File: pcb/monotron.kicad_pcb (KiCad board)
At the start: 2 copper layers, 38 parts, among them J1 Mono / Stereo, J10 DB25_Female, J11 Mini-DIN-6, J12 Mini-DIN-6, J2 AudioJack3, J3 Jack-DC, J4 DB9_Male, J5 01x07 SD Interface, J6 DB15_Female_HighDensity_Mount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, J7 2x6 UART Bridge, J8 1x4 I2C Expansion Connector, J9 DB9_Male, U1 TM4C123G_Launchpad, U2 MAX3232, U3 ATmega48A-PU

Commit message: Updated footprints.
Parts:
- added C15: 100n, Capacitor_THT:C_Disc_D5.0mm_W2.5mm_P2.50mm, F.Cu at (329.6, 106.9)
- added D1: 1N4148, Diode_THT:D_A-405_P12.70mm_Horizontal, F.Cu at (302.6, 135.2)
- added J13: DB25_Female, Connector_Dsub:DSUB-25_Male_Horizontal_P2.77x2.84mm_EdgePinOffset7.70mm_Housed_MountingHolesOffset9.12mm, F.Cu at (94.1, 144.5)
- added J14: Mini-DIN-6, Launchpad:mini-DIN 6, F.Cu at (52.7, 22.6)
- added J15: Mini-DIN-6, Launchpad:mini-DIN 6, F.Cu at (76.3, 22.7)
- added R10: 220, Resistor_THT:R_Axial_DIN0411_L9.9mm_D3.6mm_P12.70mm_Horizontal, F.Cu at (287.2, 139.8)
- added R11: 220, Resistor_THT:R_Axial_DIN0411_L9.9mm_D3.6mm_P12.70mm_Horizontal, F.Cu at (302.9, 131.5)
- added R12: 220, Resistor_THT:R_Axial_DIN0411_L9.9mm_D3.6mm_P12.70mm_Horizontal, F.Cu at (287.2, 144.0)
- added R13: 220, Resistor_THT:R_Axial_DIN0411_L9.9mm_D3.6mm_P12.70mm_Horizontal, F.Cu at (287.2, 127.4)
- added R14: 220, Resistor_THT:R_Axial_DIN0411_L9.9mm_D3.6mm_P12.70mm_Horizontal, F.Cu at (287.2, 135.7)
- added R15: 10K, Resistor_THT:R_Axial_DIN0411_L9.9mm_D3.6mm_P12.70mm_Horizontal, F.Cu at (302.9, 127.4)
- added R16: 470, Resistor_THT:R_Axial_DIN0411_L9.9mm_D3.6mm_P12.70mm_Horizontal, F.Cu at (287.2, 131.5)
- added U4: 6N138, Package_DIP:DIP-8_W7.62mm, F.Cu at (302.5, 138.4)
- added U5: ATmega48A-PU, Package_DIP:DIP-28_W7.62mm, F.Cu at (341.1, 86.7)
- C10: value 100n -> 470n
- C7: value 470n -> 100n
- J10: value DB25_Female -> DIN-5_180degree; footprint Connector_Dsub:DSUB-25_Male_Horizontal_P2.77x2.84mm_EdgePinOffset7.70mm_Housed_MountingHolesOffset9.12mm -> Launchpad:5P180 DIN Socket
- J11: value Mini-DIN-6 -> DIN-5_180degree; footprint Connector_PinHeader_2.54mm:PinHeader_1x04_P2.54mm_Horizontal -> Launchpad:5P180 DIN Socket
- J12: value Mini-DIN-6 -> DB9_Male; footprint Connector_PinHeader_2.54mm:PinHeader_1x04_P2.54mm_Horizontal -> Connector_Dsub:DSUB-9_Male_Horizontal_P2.77x2.84mm_EdgePinOffset7.70mm_Housed_MountingHolesOffset9.12mm
- J2: value AudioJack3 -> Jack-DC; footprint Connector_Audio:Jack_3.5mm_CUI_SJ1-3533NG_Horizontal -> Connector_BarrelJack:BarrelJack_CUI_PJ-102AH_Horizontal
- J3: value Jack-DC -> 01x07 SD Interface; footprint Connector_BarrelJack:BarrelJack_CUI_PJ-102AH_Horizontal -> Connector_PinHeader_2.54mm:PinHeader_1x07_P2.54mm_Vertical
- J4: value DB9_Male -> AudioJack3; footprint Connector_Dsub:DSUB-9_Male_Horizontal_P2.77x2.84mm_EdgePinOffset7.70mm_Housed_MountingHolesOffset9.12mm -> Connector_Audio:Jack_3.5mm_CUI_SJ1-3533NG_Horizontal
- J5: value 01x07 SD Interface -> DB9_Male; footprint Connector_PinHeader_2.54mm:PinHeader_1x07_P2.54mm_Vertical -> Connector_Dsub:DSUB-9_Male_Horizontal_P2.77x2.84mm_EdgePinOffset7.70mm_Housed_MountingHolesOffset9.12mm
- J6: value DB15_Female_HighDensity_MountingHoles -> 1x4 I2C Expansion Connector; footprint Connector_Dsub:DSUB-15-HD_Female_Horizontal_P2.29x1.98mm_EdgePinOffset8.35mm_Housed_MountingHolesOffset10.89mm -> Connector_PinHeader_2.54mm:PinHeader_1x04_P2.54mm_Vertical
- J7: value 2x6 UART Bridge -> DB15_Female_HighDensity_MountingHoles; footprint Connector_PinHeader_2.54mm:PinHeader_2x06_P2.54mm_Vertical -> Connector_Dsub:DSUB-15-HD_Female_Horizontal_P2.29x1.98mm_EdgePinOffset8.35mm_Housed_MountingHolesOffset10.89mm
- J8: value 1x4 I2C Expansion Connector -> 2x6 UART Bridge; footprint Connector_PinHeader_2.54mm:PinHeader_1x04_P2.54mm_Vertical -> Connector_PinHeader_2.54mm:PinHeader_2x06_P2.54mm_Vertical
- J9: value DB9_Male -> DIN-5_180degree; footprint Connector_Dsub:DSUB-9_Male_Horizontal_P2.77x2.84mm_EdgePinOffset7.70mm_Housed_MountingHolesOffset9.12mm -> Launchpad:5P180 DIN Socket
- U3: value ATmega48A-PU -> 74LS14; footprint Package_DIP:DIP-28_W7.62mm -> Package_DIP:DIP-14_W7.62mm
- moved J10 242.3 mm to (18.2, 150.1)
- moved J3 219.3 mm to (-34.4, 86.4)
- moved J11 175.0 mm to (40.0, 149.5)
- moved J4 140.7 mm to (105.4, 94.7), turned to 270 degrees
- moved J7 140.3 mm to (92.1, 68.7), turned to 90 degrees
- moved J12 104.3 mm to (94.1, 179.2)
- moved J5 64.1 mm to (93.9, 45.3), turned to 90 degrees
- moved C10 59.1 mm to (185.1, 111.1)
- moved C1 59.1 mm to (202.0, 108.2)
- moved C2 59.1 mm to (207.5, 108.2)
- moved C8 59.1 mm to (196.2, 111.1)
- moved C9 59.1 mm to (190.6, 111.1)
- moved U1 51.1 mm to (57.5, 99.3)
- moved C12 46.0 mm to (143.4, 148.3)
- moved C14 35.9 mm to (122.8, 164.6)
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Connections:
- net Net-(R3-Pad1) renamed /PE4_AUDIO_L
- net Net-(R4-Pad1) renamed /PE5_AUDIO_R
- net Net-(U1-Pad2.2) renamed /PB2_SPARE
- net Net-(U1-Pad2.4) renamed /BUTTON_1
- net Net-(U1-Pad2.7) renamed /PB6_SPARE
- net Net-(U1-Pad3.5) renamed /PD2_SPARE
- net Net-(U1-Pad4.1) renamed /BLUE_LED
- net Net-(U1-Pad4.2) renamed /GREEN_LED
- net Net-(U1-Pad4.3) renamed /PB3_SPARE
- C10 pad 1: Net-(C10-Pad1) -> GND
- C10 pad 2: GND -> Net-(C10-Pad2)
- C7 pad 2: Net-(C7-Pad2) -> GND
- C8 pad 1: Net-(C10-Pad1) -> Net-(C8-Pad1)
- C9 pad 1: GND -> Net-(C7-Pad1)
- J10 pad 1: /Monotron I/O Expansion/STROBE -> Net-(J10-Pad1)
- J10 pad 2: /Monotron I/O Expansion/D0 -> GND
- J10 pad 3: /Monotron I/O Expansion/D1 -> Net-(J10-Pad3)
- J10 pad 4: /Monotron I/O Expansion/D2 -> Net-(J10-Pad4)
- J10 pad 5: /Monotron I/O Expansion/D3 -> Net-(J10-Pad5)
- J10 pad 6: /Monotron I/O Expansion/D4 -> (no net)
- J10 pad 7: /Monotron I/O Expansion/D5 -> (no net)
- J11 pad 1: /Monotron I/O Expansion/KB_DATA -> Net-(J11-Pad1)
- J11 pad 3: GND -> Net-(J11-Pad3)
- J11 pad 4: +5V -> Net-(J11-Pad4)
- J12 pad 1: /Monotron I/O Expansion/MS_DATA -> /DCD
- J12 pad 2: Net-(J12-Pad2) -> /RS232_RX
- J12 pad 3: GND -> /RS232_TX
- J12 pad 4: +5V -> /DTR
- J3 pad 1: +5V -> Net-(J3-Pad1)
- J3 pad 2: GND -> /PA4_SD_MISO
- J3 pad 3: (no net) -> GND
- J5 pad 1: Net-(J5-Pad1) -> /PE2_JS_UP
- J5 pad 2: /PA4_SD_MISO -> /PE3_JS_DOWN
- J5 pad 3: GND -> /PD6_JS_LEFT
- J5 pad 4: /PA2_SD_CLK -> /PD7_JS_RIGHT
- J5 pad 5: +3V3 -> Net-(J5-Pad5)
- J5 pad 6: /PA5_SD_MOSI -> /PF4_JS_FIRE
- J5 pad 7: /PA3_SD_CS -> Net-(J5-Pad7)
- J6 pad 1: Net-(J6-Pad1) -> GND
- J6 pad 2: Net-(J6-Pad2) -> +5V
- J6 pad 3: Net-(J6-Pad3) -> /PA7_I2C_SDA
- J6 pad 4: Net-(J6-Pad4) -> /PA6_I2C_SCL
- J7 pad 1: +3V3 -> Net-(J7-Pad1)
- J7 pad 10: /DTE_CTS -> Net-(J7-Pad10)
- J7 pad 11: GND -> Net-(J7-Pad11)
- J7 pad 12: GND -> Net-(J7-Pad12)
- J7 pad 2: Net-(C10-Pad1) -> Net-(J7-Pad2)
- J7 pad 3: /PB0_U1RX -> Net-(J7-Pad3)
- J7 pad 4: /DTE_RX -> Net-(J7-Pad4)
- J7 pad 5: /PB1_U1TX -> GND
- J7 pad 6: /DTE_TX -> GND
- J7 pad 7: /PC4_U1RTS -> GND
- J7 pad 8: /DTE_RTS -> GND
- J7 pad 9: /PC5_U1CTS -> Net-(J7-Pad9)
- J8 pad 1: GND -> +3V3
- J8 pad 2: +5V -> Net-(C7-Pad1)
- J8 pad 3: /PA7_I2C_SDA -> /PB0_U1RX
- J8 pad 4: /PA6_I2C_SCL -> /DTE_RX
- J9 pad 1: /DCD -> Net-(J9-Pad1)
- J9 pad 2: /RS232_RX -> GND
- J9 pad 3: /RS232_TX -> Net-(J9-Pad3)
- J9 pad 4: /DTR -> Net-(J9-Pad4)
- J9 pad 5: GND -> Net-(J9-Pad5)
- J9 pad 6: /DSR -> (no net)
- J9 pad 7: /RS232_RTS -> (no net)
- R7 pad 1: Net-(J6-Pad1) -> Net-(J7-Pad1)
- R8 pad 1: Net-(J6-Pad2) -> Net-(J7-Pad2)
- R9 pad 1: Net-(J6-Pad3) -> Net-(J7-Pad3)
- U1 pad 3.8: Net-(U1-Pad3.8) -> /PE2_JS_UP
- U1 pad 3.9: Net-(U1-Pad3.9) -> /PE3_JS_DOWN
- U1 pad 4.10: /PF4_FIRE -> /PF4_JS_FIRE
- U1 pad 4.6: /PC6_UP -> /PC6_MIDI_IN
- U1 pad 4.7: /PC7_DOWN -> /PC7_MIDI_OUT
- U1 pad 4.8: /PD6_LEFT -> /PD6_JS_LEFT
- U1 pad 4.9: /PD7_RIGHT -> /PD7_JS_RIGHT
- U2 pad 16: Net-(C10-Pad1) -> Net-(C7-Pad1)
- U2 pad 2: Net-(C8-Pad2) -> Net-(C9-Pad2)
- U2 pad 4: Net-(C7-Pad1) -> Net-(C8-Pad1)
- U2 pad 5: Net-(C7-Pad2) -> Net-(C8-Pad2)
- U2 pad 6: Net-(C9-Pad2) -> Net-(C10-Pad2)
- U3 pad 1: /Monotron I/O Expansion/SELPRIN -> /PC6_MIDI_IN
- U3 pad 10: /Monotron I/O Expansion/D7 -> (no net)
- U3 pad 11: /Monotron I/O Expansion/SEL -> (no net)
- U3 pad 12: /Monotron I/O Expansion/STROBE -> (no net)
- U3 pad 13: /Monotron I/O Expansion/AUTOF -> (no net)
- U3 pad 14: /Monotron I/O Expansion/D0 -> +5V
- U3 pad 2: /PE1_U7TX -> Net-(U3-Pad2)
- U3 pad 3: /PE0_U7RX -> Net-(U3-Pad2)
- U3 pad 4: /Monotron I/O Expansion/ACK -> Net-(R12-Pad1)
- U3 pad 5: /Monotron I/O Expansion/BUSY -> Net-(U3-Pad5)
- U3 pad 6: /Monotron I/O Expansion/PE -> Net-(R13-Pad2)
- U3 pad 7: +5V -> GND
- U3 pad 8: GND -> Net-(U3-Pad5)
- U3 pad 9: /Monotron I/O Expansion/D6 -> /PC7_MIDI_OUT

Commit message: Primary component layout complete.
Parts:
- removed C15: 100n, Capacitor_THT:C_Disc_D5.0mm_W2.5mm_P2.50mm
- J10: value DIN-5_180degree -> DIN5 MIDI Thru
- J11: value DIN-5_180degree -> DIN5 MIDI In
- J12: value DB9_Male -> DE9 RS232
- J5: value DB9_Male -> DE9 Joystick
- J7: value DB15_Female_HighDensity_MountingHoles -> DE15HD VGA
- J9: value DIN-5_180degree -> DIN5 MIDI Out
- moved U5 250.4 mm to (91.5, 107.8), turned to 90 degrees
- moved R15 203.1 mm to (100.0, 136.7), turned to 90 degrees
- moved J3 190.3 mm to (146.3, 145.7), turned to 90 degrees
- moved R4 187.8 mm to (52.0, 141.7), turned to 90 degrees
- moved R13 185.1 mm to (104.3, 155.7), turned to 180 degrees
- moved R16 182.4 mm to (104.8, 133.7)
- moved D1 179.0 mm to (124.3, 119.2), turned to 180 degrees
- moved U4 172.8 mm to (130.3, 123.7), turned to 270 degrees
- moved J9 167.5 mm to (117.3, 167.2)
- moved R10 162.9 mm to (124.3, 137.0), turned to 270 degrees
- moved R14 156.4 mm to (130.8, 137.2), turned to 270 degrees
- moved J6 155.1 mm to (142.3, 133.7), turned to 180 degrees
- moved R11 154.3 mm to (149.8, 151.2)
- moved J14 153.9 mm to (75.8, 174.7), turned to 180 degrees
- moved J15 153.5 mm to (97.6, 174.7), turned to 180 degrees
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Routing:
- net Net-(J7-Pad1): track 0.00 -> 9.97 mm
- net Net-(J7-Pad2): track 0.00 -> 8.42 mm
- net +5V: track 0.00 -> 5.94 mm
- net Net-(J7-Pad3): track 0.00 -> 5.86 mm
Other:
- board outline added: 135 x 102.5 mm

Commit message: Fun with routing!
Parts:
- moved J9 58.3 mm to (163.3, 131.4)
- moved R13 58.3 mm to (150.3, 119.9)
- moved R16 58.3 mm to (150.8, 97.9)
- moved U3 58.3 mm to (163.3, 102.9)
- moved J10 58.3 mm to (201.3, 131.4)
- moved J11 58.3 mm to (182.3, 131.4)
- moved J14 58.3 mm to (121.8, 138.9)
- moved J15 58.3 mm to (143.6, 138.9)
- moved J3 58.3 mm to (192.3, 109.9)
- moved R11 58.3 mm to (195.8, 115.4)
- moved R12 58.3 mm to (183.3, 101.4)
- moved R14 58.3 mm to (176.8, 101.4)
- moved C11 58.3 mm to (153.3, 85.9)
- moved C13 58.3 mm to (152.8, 74.7)
- moved D1 58.3 mm to (170.3, 83.4)
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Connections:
- U5 pad 11: /Monotron I/O Expansion/SEL -> /Monotron I/O Expansion/ERROR
- U5 pad 27: /Monotron I/O Expansion/ERROR -> /Monotron I/O Expansion/INIT
- U5 pad 28: /Monotron I/O Expansion/INIT -> /Monotron I/O Expansion/SEL
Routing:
- net GND: track 0.00 -> 455.4 mm
- net /PC5_U1CTS: track 0.00 -> 286.8 mm
- net /PC4_U1RTS: track 0.00 -> 118.2 mm, vias 0 -> 1
- net /PD6_JS_LEFT: track 0.00 -> 116.0 mm
- net /PB1_U1TX: track 0.00 -> 110.9 mm, vias 0 -> 3
- net /PF4_JS_FIRE: track 0.00 -> 103.7 mm, vias 0 -> 1
- net /PB5_VGA_VSYNC: track 0.00 -> 80.8 mm
- net /PF1_VGA_RED: track 0.00 -> 73.3 mm
- net /PD7_JS_RIGHT: track 0.00 -> 66.1 mm
- net /PE3_JS_DOWN: track 0.00 -> 64.7 mm
- net /PE2_JS_UP: track 0.00 -> 58.8 mm
- net +3V3: track 0.00 -> 56.3 mm
- net +5V: track 5.94 -> 57.3 mm, vias 0 -> 1
- net /PE1_U7TX: track 0.00 -> 46.0 mm
- net /Monotron I/O Expansion/SELPRIN: track 0.00 -> 45.4 mm
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
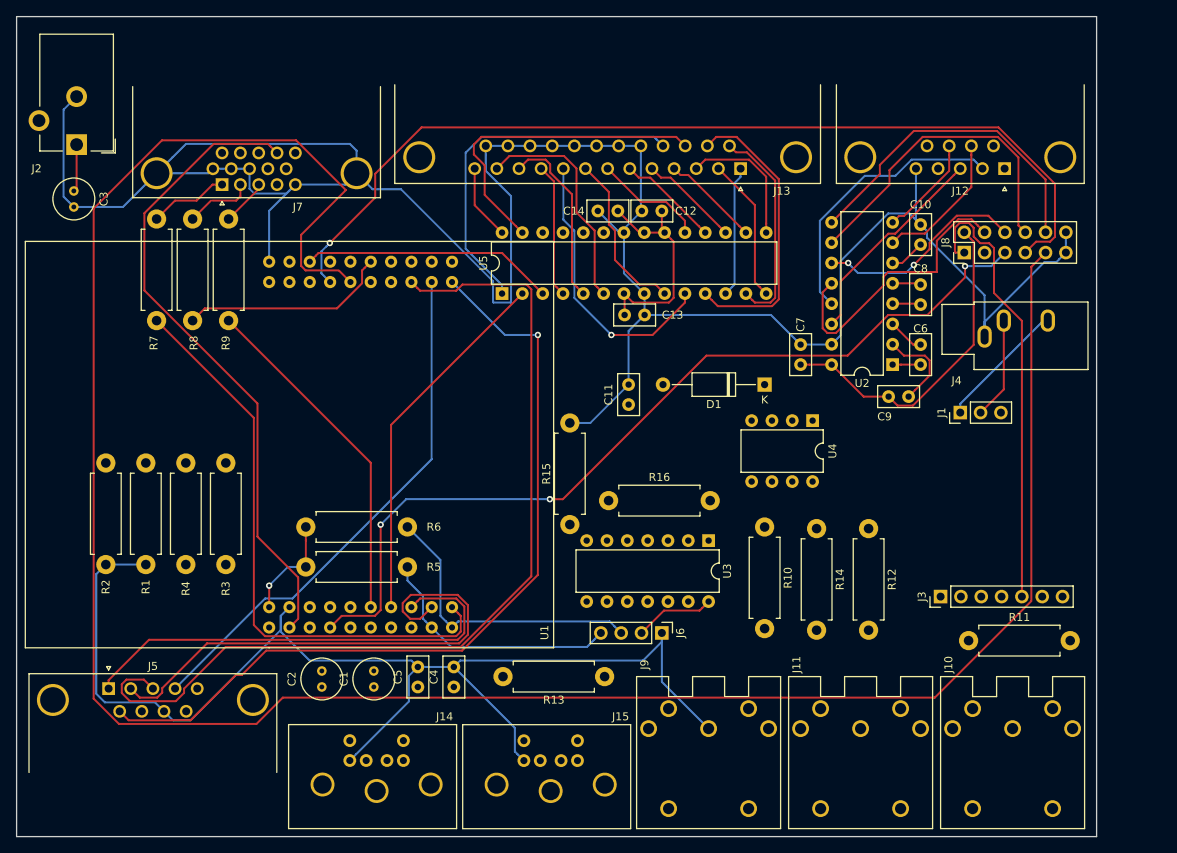
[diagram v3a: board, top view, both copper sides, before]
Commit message: Moved some pins around to ease the routing.
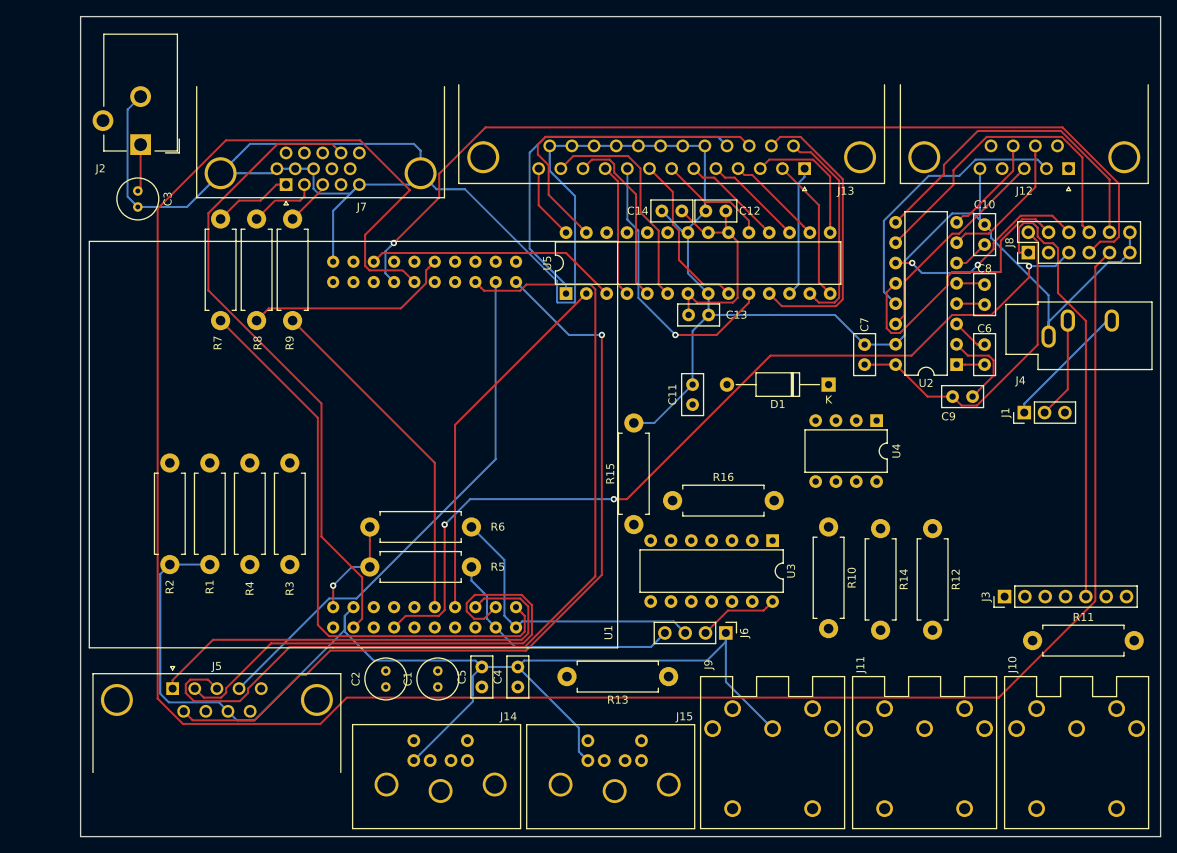
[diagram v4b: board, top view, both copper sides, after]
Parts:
- moved J14 8.00 mm to (129.8, 138.9)
- moved C1 8.00 mm to (129.5, 121.2)
- moved C10 8.00 mm to (197.8, 63.4)
- moved C11 8.00 mm to (161.3, 85.9)
- moved C12 8.00 mm to (165.5, 61.7)
- moved C13 8.00 mm to (160.8, 74.7)
- moved C14 8.00 mm to (160.0, 61.7)
- moved C2 8.00 mm to (123.0, 121.2)
- moved C3 8.00 mm to (92.0, 59.2)
- moved C4 8.00 mm to (139.5, 121.2)
- moved C5 8.00 mm to (135.0, 121.2)
- moved C6 8.00 mm to (197.8, 80.9)
- moved C7 8.00 mm to (182.8, 80.9)
- moved C8 8.00 mm to (197.8, 73.4)
- moved C9 8.00 mm to (193.8, 84.9)
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
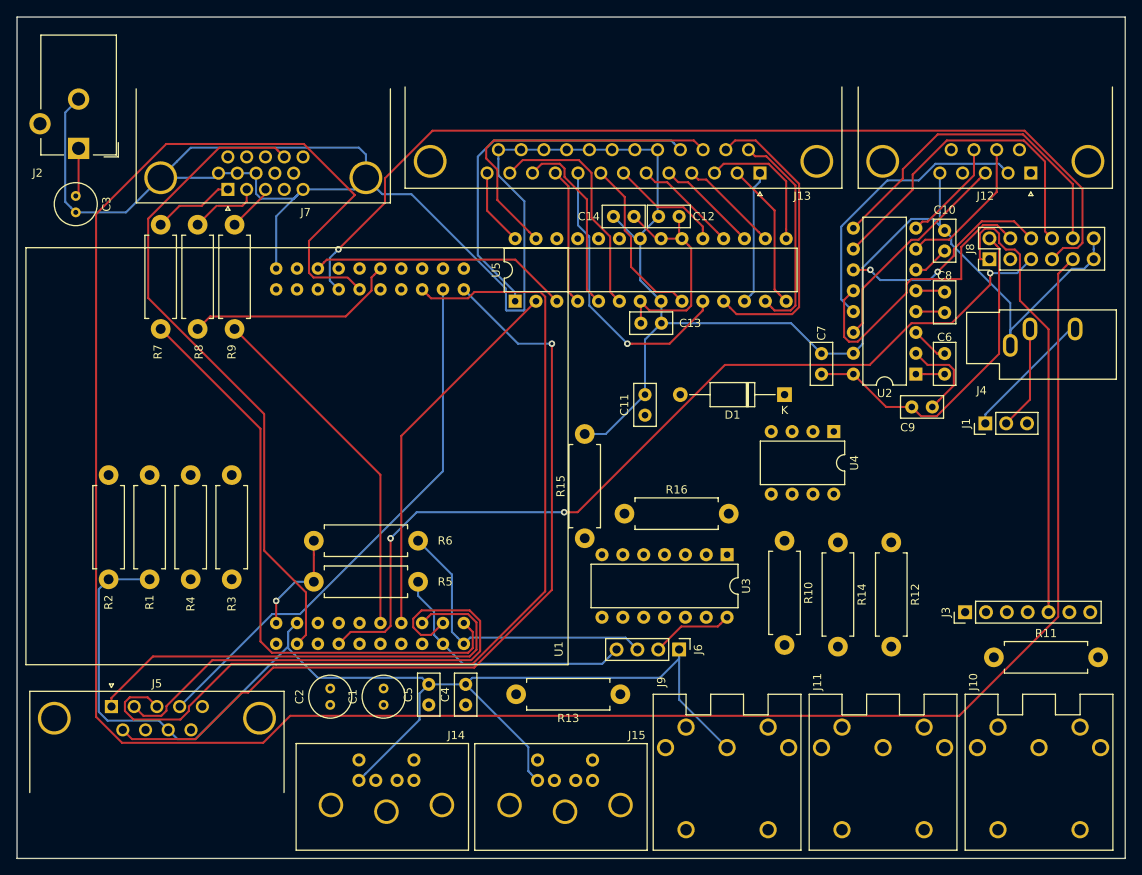
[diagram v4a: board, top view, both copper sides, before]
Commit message: Shrunk board a little (components can hang off edge). Relabelled parts to generic names.
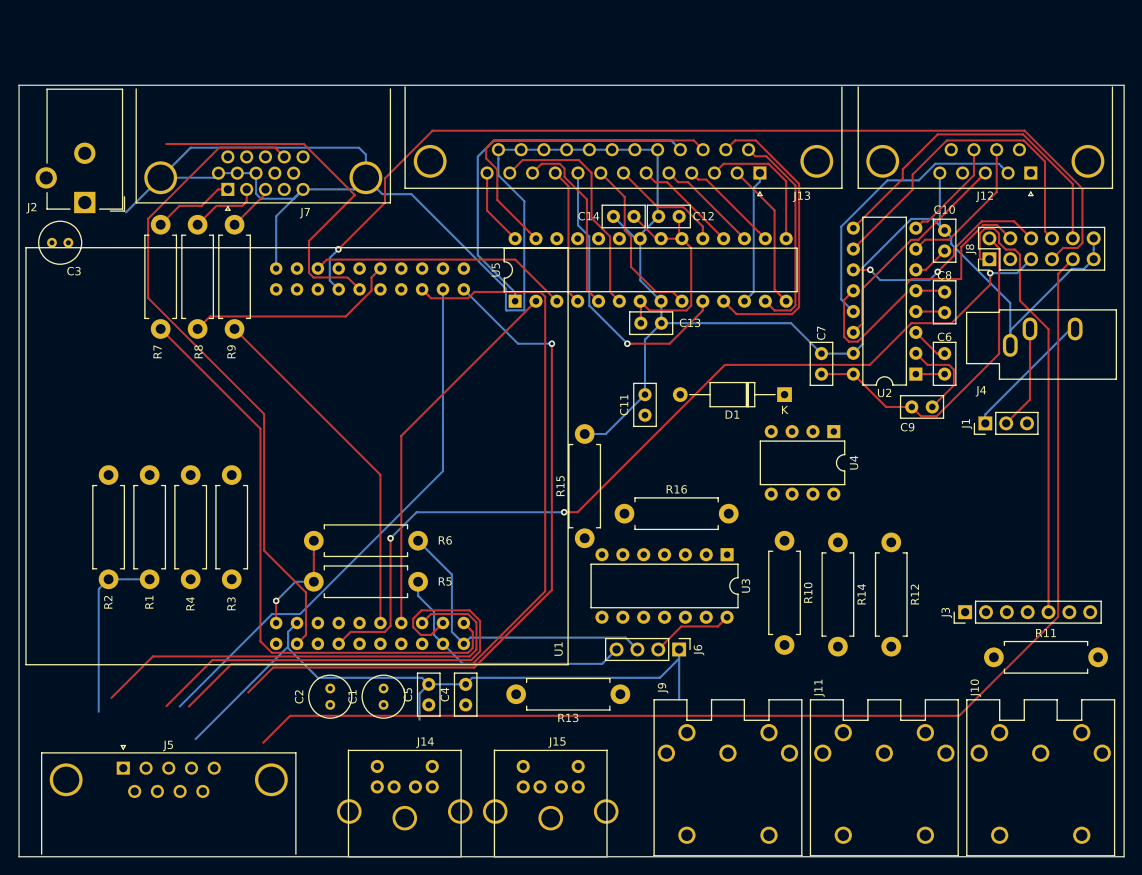
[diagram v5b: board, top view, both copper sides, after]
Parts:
- J10: value DIN5 MIDI Thru -> DIN5-180
- J11: value DIN5 MIDI In -> DIN5-180
- J12: value DE9 RS232 -> DE9M
- J14, J15: footprint Launchpad:mini-DIN 6 -> Monotron:mini-DIN 6
- J3: value 01x07 SD Interface -> 1x7 Header
- J5: value DE9 Joystick -> DE9F
- J6: value 1x4 I2C Expansion Connector -> 1x4 Header
- J7: value DE15HD VGA -> DE15HD
- J8: value 2x6 UART Bridge -> 2x6 Header
- J9: value DIN5 MIDI Out -> DIN5-180
- moved J5 7.64 mm to (97.8, 128.9)
- moved J2 6.64 mm to (93.1, 60.0)
- moved C3 6.40 mm to (89.1, 64.9), turned to 0 degrees
- moved J14 2.37 mm to (132.1, 139.7)
- moved J15 1.91 mm to (149.9, 139.7)
- moved J10 0.71 mm to (209.6, 132.1)
- moved J11 0.69 mm to (190.5, 132.1)
- moved J9 0.68 mm to (171.4, 132.1)
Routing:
- net /PC5_U1CTS: track 286.8 -> 191.8 mm
- net GND: track 455.4 -> 387.1 mm
- net /PF4_JS_FIRE: track 103.7 -> 85.6 mm
- net /PD6_JS_LEFT: track 116.0 -> 101.1 mm
- net +5V: track 57.3 -> 51.3 mm
- net /PE3_JS_DOWN: track 64.7 -> 59.4 mm
- net /PE2_JS_UP: track 58.8 -> 57.7 mm
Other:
- board size 135 x 102.5 mm -> 134.6 x 94 mm
